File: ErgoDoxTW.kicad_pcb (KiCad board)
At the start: 2 copper layers, 182.8 x 158.9 mm, 72 parts, among them J1 3.5mm, P1 hole_r1.75, P2 hole_r1.75, P3 hole_r1.75, P4 hole_r1.75, P5 hole_r1.75, P6 hole_r1.75, P7 hole_r1.75, P8 hole_r1.75, SW0:10 SW0:3, SW0:11 SW0:2, SW0:12 SW0:1, SW0:7 SW0:6, SW0:8 SW0:5, SW0:9 SW0:4, SW1:10 SW1:3, SW1:11 SW1:2, SW1:12 SW1:1, SW1:13 SW1:0, SW1:9 SW1:4, SW2:10 SW2:3, SW2:11 SW2:2, SW2:12 SW2:1, SW2:13 SW2:0, SW2:7 SW2:6, SW2:8 SW2:5, SW2:9 SW2:4, SW3:10 SW3:3, SW3:11 SW3:2, SW3:12 SW3:1, SW3:13 SW3:0, SW3:8 SW3:5, SW3:9 SW3:4, SW4:10 SW4:3, SW4:11 SW4:2, SW4:12 SW4:1, SW4:13 SW4:0, SW4:7 SW4:6, SW4:8 SW4:5, SW4:9 SW4:4, SW5:10 SW5:3, SW5:11 SW5:2, SW5:12 SW5:1, SW5:13 SW5:0, SW5:7 SW5:6, SW5:8 SW5:5, SW5:9 SW5:4, U2 MCP23018, U4 TEENSY2.0

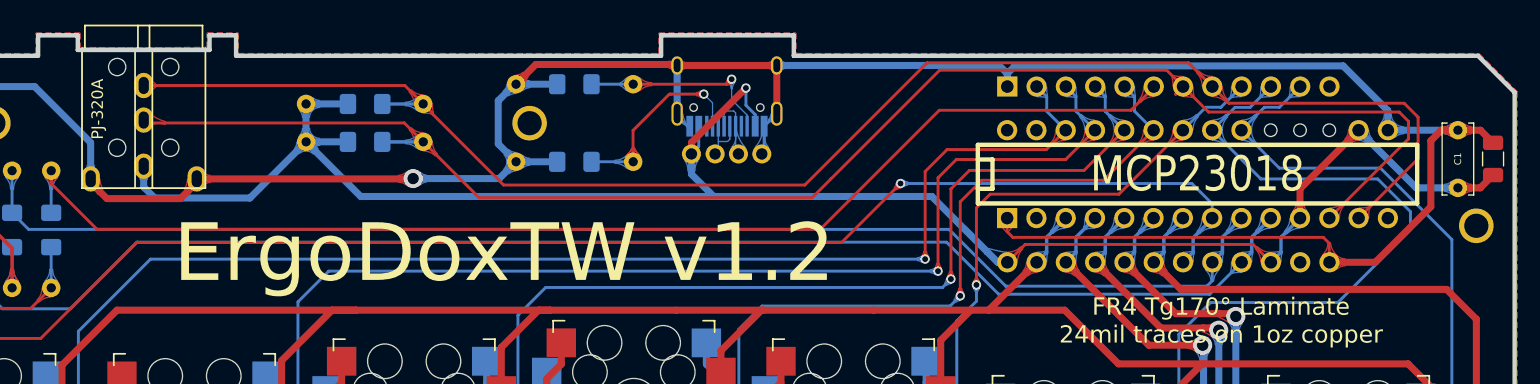
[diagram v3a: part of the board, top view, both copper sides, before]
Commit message: update v1.3
support PJ-320E 3.5mm audio jack
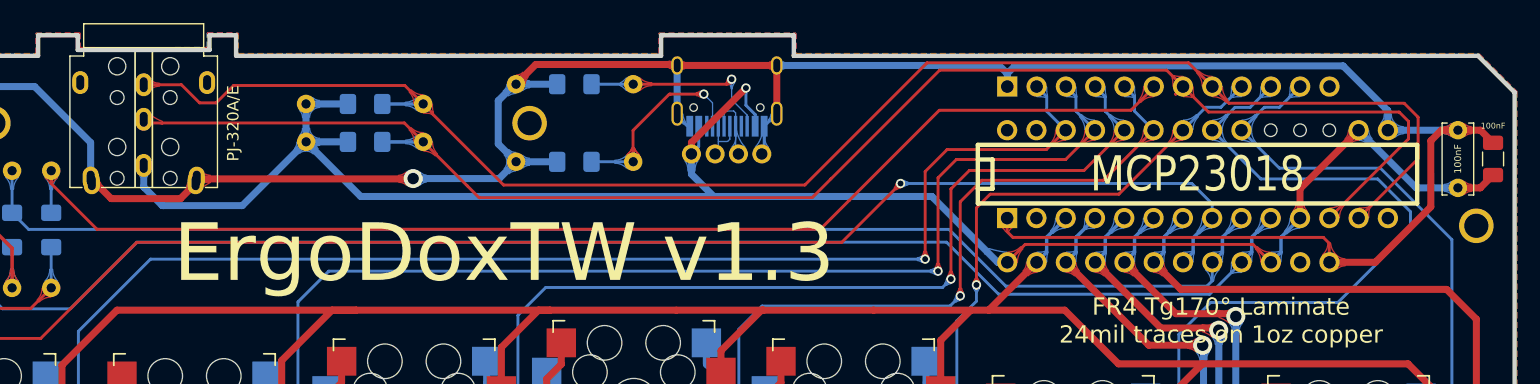
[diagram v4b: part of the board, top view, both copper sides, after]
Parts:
- removed C2: 100nF, Capacitor_SMD:C_1206_3216Metric
- added 100nF: 100nF, Capacitor_SMD:C_1206_3216Metric, F.Cu at (204.0, 41.2)
- J1: footprint Enhance:PJ-320A-Dual -> Enhance:PJ-320A_and_320E-Dual
- moved J1 0.07 mm to (87.0, 31.6)
- renumbered C1 to 100nF
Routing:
- net /SDAM: track 134.9 -> 136.2 mm
- net GND: track 252.7 -> 253.7 mm
- net VCC: track 165.3 -> 165.8 mm
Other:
- board text added: "ErgoDoxTW v1.3"
- board text removed: "ErgoDoxTW v1.2"
